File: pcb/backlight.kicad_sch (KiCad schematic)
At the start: 52 parts, among them U1 AL8860WT, U3 AL8860WT, U4 AL8860WT

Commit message: PCB for 4x5 scanlight
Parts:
- removed C1, C3, C6: 10u, Capacitor_SMD:C_1210_3225Metric, symbol Device:C
- removed C2, C5: 1u, Capacitor_SMD:C_0603_1608Metric, symbol Device:C
- removed D1, D2, D3, D4, D5, D6: deep blue, LED_SMD:LED_PLCC_2835_Handsoldering, symbol Device:LED
- removed D10, D11, D12, D13, D14, D9: green, LED_SMD:LED_PLCC_2835_Handsoldering, symbol Device:LED
- removed D15, D7, D8: B240A, Diode_SMD:D_SMA, symbol Diode:MBRA340
- removed D16, D17, D18, D19, D20, D21: deep red, LED_SMD:LED_PLCC_2835_Handsoldering, symbol Device:LED
- removed L1, L2, L3: 100u, Inductor_SMD:L_Bourns_SRN8040TA, symbol Device:L
- removed R1, R10, R11, R12, R4, R9: 1.4, Resistor_SMD:R_1206_3216Metric, symbol Device:R_US
- removed R2, R3, R5: 649k, Resistor_SMD:R_0603_1608Metric, symbol Device:R_US
- removed RV1, RV2, RV3: 100k, Potentiometer_THT:Potentiometer_Bourns_PTV09A-1_Single_Vertical, symbol Device:R_Potentiometer_US
- removed U1, U3, U4: AL8860WT, Package_TO_SOT_SMD:TSOT-23-5, symbol Driver_LED:AL8860WT
- added C11, C13: 47n, Capacitor_SMD:C_0805_2012Metric, symbol Device:C
- added C6: 0.1u, Capacitor_SMD:C_0603_1608Metric, symbol Device:C_Small
- added J2: SWD_TC2030, Connector:Tag-Connect_TC2030-IDC-NL_2x03_P1.27mm_Vertical, symbol Connector:Conn_ARM_SWD_TagConnect_TC2030-NL
- added R2: 100k, Resistor_SMD:R_0603_1608Metric, symbol Device:R_Small
- added R5, R7, R8: 4.7k, Resistor_SMD:R_0603_1608Metric, symbol Device:R
- added SW1: BOOT, Jumper:SolderJumper-2_P1.3mm_Open_TrianglePad1.0x1.5mm, symbol Switch:SW_SPST
- added SW2: RotaryEncoder_Switch_MP, Rotary_Encoder:RotaryEncoder_Alps_EC11E-Switch_Vertical_H20mm, symbol Device:RotaryEncoder_Switch_MP
- added U1: 0.91 Inch OLED, Display:0.91_Inch_OLED, symbol Display_Graphic:0.91_Inch_OLED
- added U3: STM32G0B1CBUx, Package_DFN_QFN:QFN-48-1EP_7x7mm_P0.5mm_EP5.6x5.6mm, symbol MCU_ST_STM32G0:STM32G0B1CBUx
- C7: value 1u -> 47n; footprint Capacitor_SMD:C_0603_1608Metric -> Capacitor_SMD:C_0805_2012Metric; MPN Generic 1uF 25V 0603 X7R -> Generic 0.047uF 50V X7R 0805
- H1: renamed from H5; footprint Custom:MountingHole_2.2mm_M2_Mask_5mm -> MountingHole:MountingHole_2.2mm_M2_Mask_5mm; now left out of the parts list
- H2: renamed from H6; footprint Custom:MountingHole_2.2mm_M2_Mask_5mm -> MountingHole:MountingHole_2.2mm_M2_Mask_5mm; now left out of the parts list
- H3, H4: footprint Custom:MountingHole_2.2mm_M2_Mask_5mm -> MountingHole:MountingHole_2.2mm_M2_Mask_5mm; now left out of the parts list
- H5: renamed from H1; footprint Custom:MountingHole_2.2mm_M2_Mask_5mm -> MountingHole:MountingHole_2.2mm_M2_Mask_5mm; now left out of the parts list
- H6: renamed from H2; footprint Custom:MountingHole_2.2mm_M2_Mask_5mm -> MountingHole:MountingHole_2.2mm_M2_Mask_5mm; now left out of the parts list
- SYM1: renamed from SYM101; footprint Custom:hot-surface_1x -> Symbol:HOT; now left out of the parts list
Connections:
- net GND: now also C7.2, C11.2, C13.2, C6.2, J2.5 (GND), R2.2, SW2.C, SW2.MP, SW2.S2, U1.1 (GND), U3.49 (VSS), U3.7 (VSS)
- net CTRL_R: now reaches C7.1
- net CTRL_R: now also R5.1
- new net +3.3V: C6.1, J2.1 (VCC), SW1.2 (B), U1.2 (VCC), U3.4 (VBAT), U3.5 (VREF+), U3.6 (VDD)
- new net ADC_VBUS: U3.22 (PB10)
- new net CC1: U3.28 (PA8)
- new net CC2: U3.27 (PB15)
- new net CTRL_B: C13.1, R8.1
- new net CTRL_G: C11.1, R7.1
- new net D+: U3.34 (PA10/PA12)
- new net D-: U3.33 (PA9/PA11)
- new net NRST: J2.3 (~{RESET}), U3.10 (PF2)
- new net PWM_B: R8.2, U3.13 (PA2)
- new net PWM_G: R7.2, U3.12 (PA1)
- new net PWM_R: R5.2, U3.11 (PA0)
- new net R_I: SW2.B, U3.16 (PA5)
- new net R_Q: SW2.A, U3.15 (PA4)
- new net R_SW: SW2.S1, U3.14 (PA3)
- new net SCL: U1.3 (SCL), U3.18 (PA7)
- new net SDA: U1.4 (SDA), U3.17 (PA6)
- new net SWCLK: J2.4 (SWCLK), R2.1, SW1.1 (A), U3.36 (PA14)
- new net SWDIO: J2.2 (SWDIO), U3.35 (PA13)
- new net ~{DB}: U3.30 (PC6)
- new net ~{FLT}: U3.29 (PA9/UCPD1_DBCC1)
- no-connect marks 0 -> 1
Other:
- removed sheet power input
- added sheet LED_Blue1 (leds.kicad_sch)
- added sheet LED_Blue2 (leds.kicad_sch)
- added sheet LED_Green1 (leds.kicad_sch)
- added sheet LED_Green2 (leds.kicad_sch)
- added sheet LED_Red1 (leds.kicad_sch)
- added sheet LED_Red2 (leds.kicad_sch)
- added sheet Power (power.kicad_sch)
- note removed: "CTRL range: 0-2.5V"
- note removed: "I=0.1/R_s"
- note removed: "Input: 19-24V"
- note removed: "WARNING: most (all?) 2835 package deep red (and some deep blue) LEDs have reversed polarity for some reason! check datasheet before assembling!"
- moved on the sheet: H1, H2, H3, H4, H5, H6

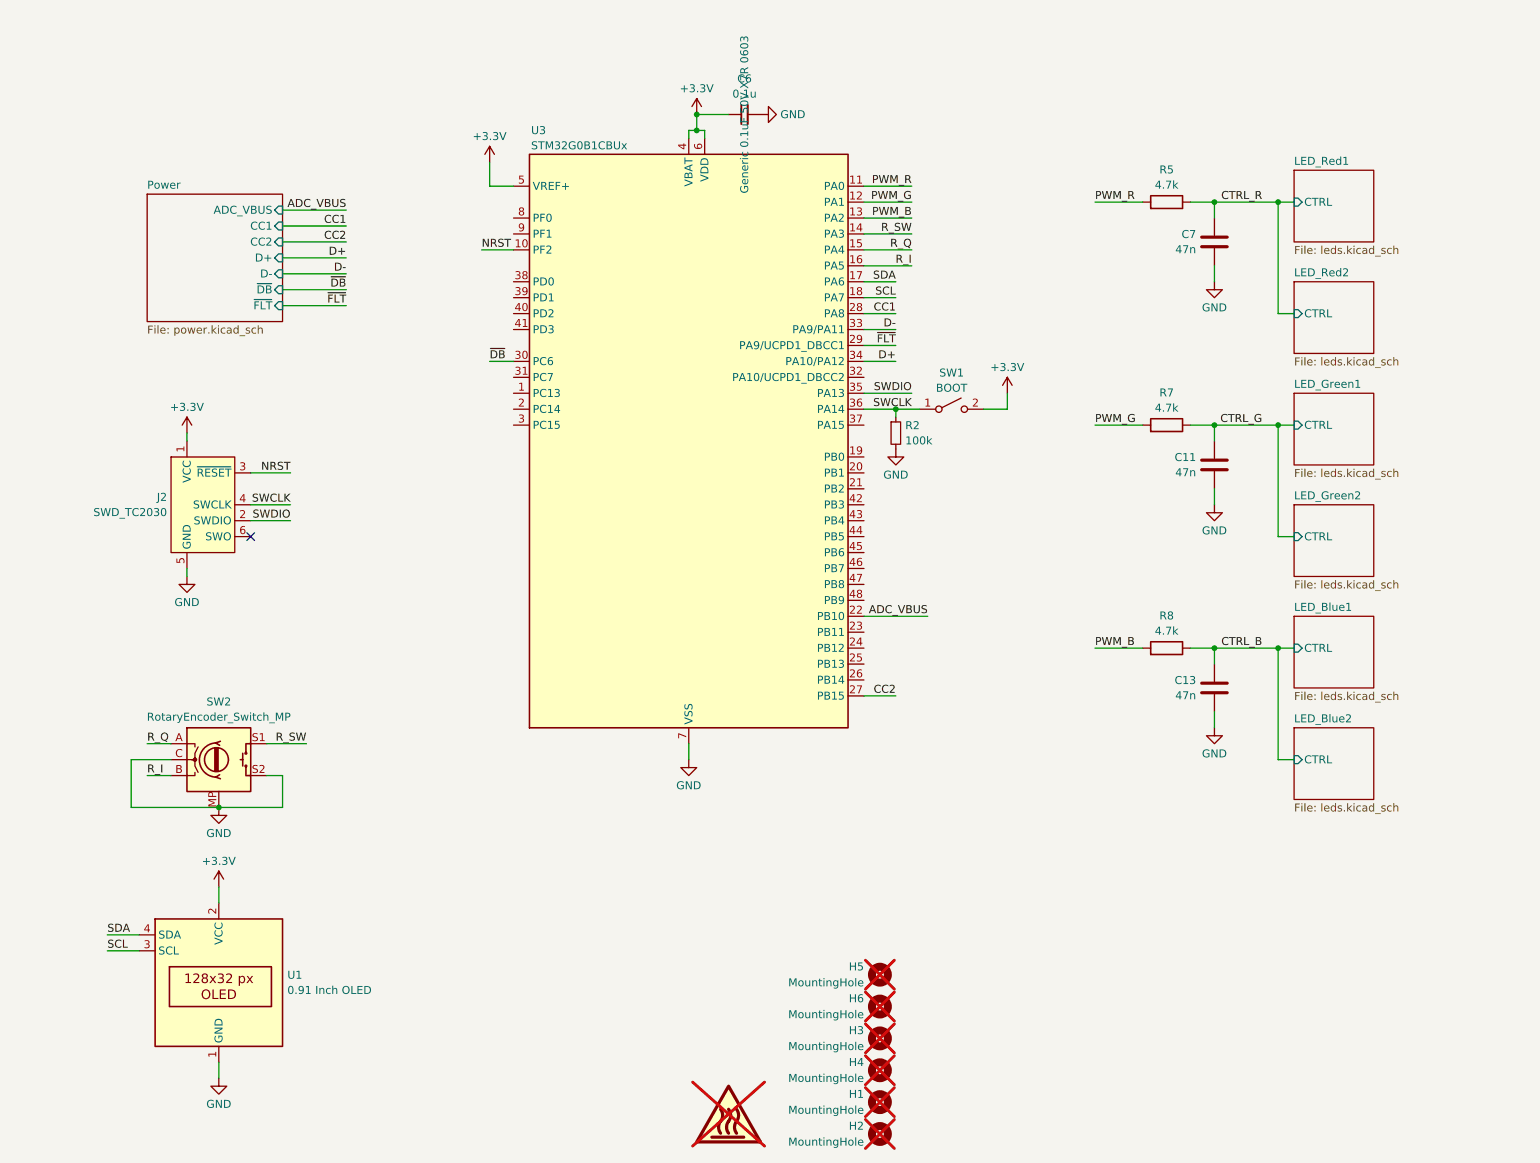
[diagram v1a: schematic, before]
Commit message: finalized schematic v2, add GS cap for inrush current
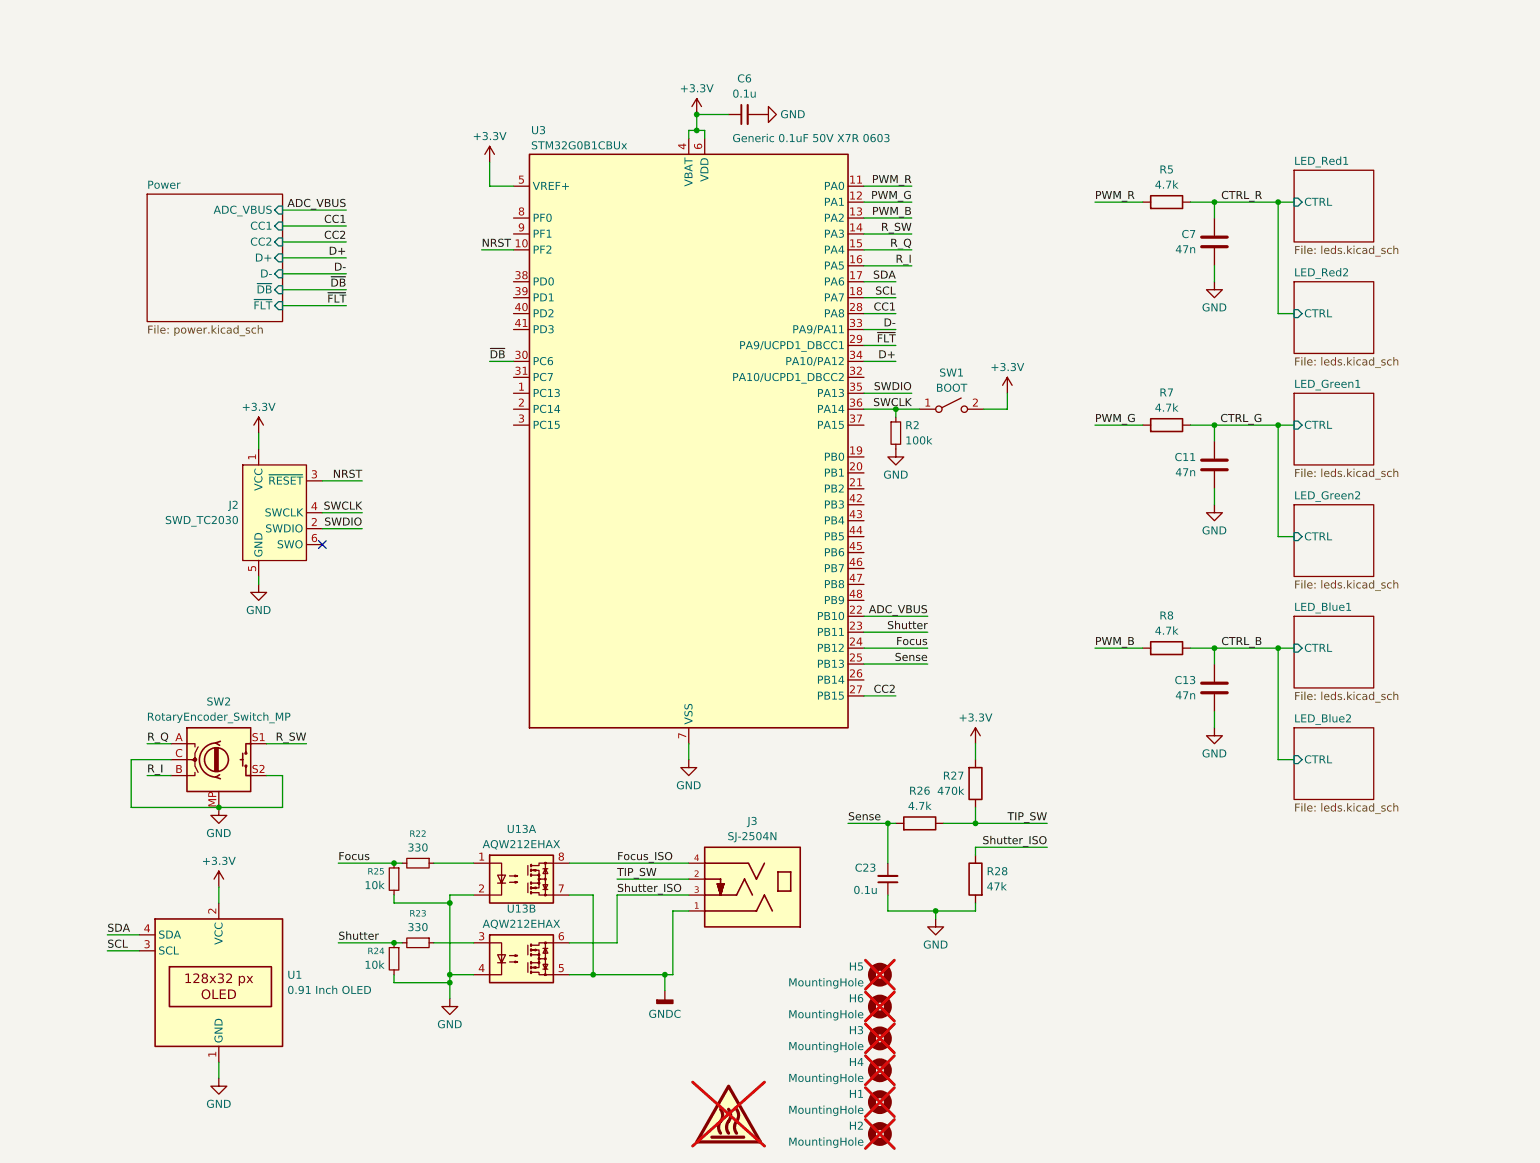
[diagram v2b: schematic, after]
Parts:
- added C23: 0.1u, Capacitor_SMD:C_0603_1608Metric, symbol Device:C_Small
- added J3: SJ-2504N, SJ-2504N:CUI_SJ-2504N, symbol SJ-2504N:SJ-2504N
- added R22, R23: 330, Resistor_SMD:R_0603_1608Metric, symbol Device:R_Small
- added R24, R25: 10k, Resistor_SMD:R_0603_1608Metric, symbol Device:R_Small
- added R26: 4.7k, Resistor_SMD:R_0603_1608Metric, symbol Device:R
- added R27: 470k, Resistor_SMD:R_0603_1608Metric, symbol Device:R
- added R28: 47k, Resistor_SMD:R_0603_1608Metric, symbol Device:R
- added U13: AQW212EHAX, Custom:DIP-8_W8.3_SMDSocket, symbol Relay_SolidState:AQW212EHAX
- U1: footprint Display:0.91_Inch_OLED -> Custom:0.91_OLED_Display
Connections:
- net +3.3V: now also R27.2
- net GND: now also C23.1, R24.2, R25.2, R28.2, U13.2, U13.4
- net Shutter: now reaches U3.23 (PB11)
- net Shutter: now also R23.2, R24.1
- net Focus: now reaches U3.24 (PB12)
- net Focus: now also R22.2, R25.1
- net Sense: now reaches U3.25 (PB13)
- net Sense: now also C23.2, R26.2
- new net: R23.1, U13.3
- new net: R22.1, U13.1
- new net Focus_ISO: J3.4, U13.8
- new net GNDC: J3.1, U13.5, U13.7
- new net Shutter_ISO: J3.3, R28.1, U13.6
- new net TIP_SW: J3.2, R26.1, R27.1
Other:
- moved on the sheet: J2
